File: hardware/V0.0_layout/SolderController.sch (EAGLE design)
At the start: 41 parts, among them IC3 TC10553.3V, J1 12V input, Q1 16MHz, SW1 ENCODER_SW1-PEC12, U1 ATMEGA328P-AU(R), U3 78M05

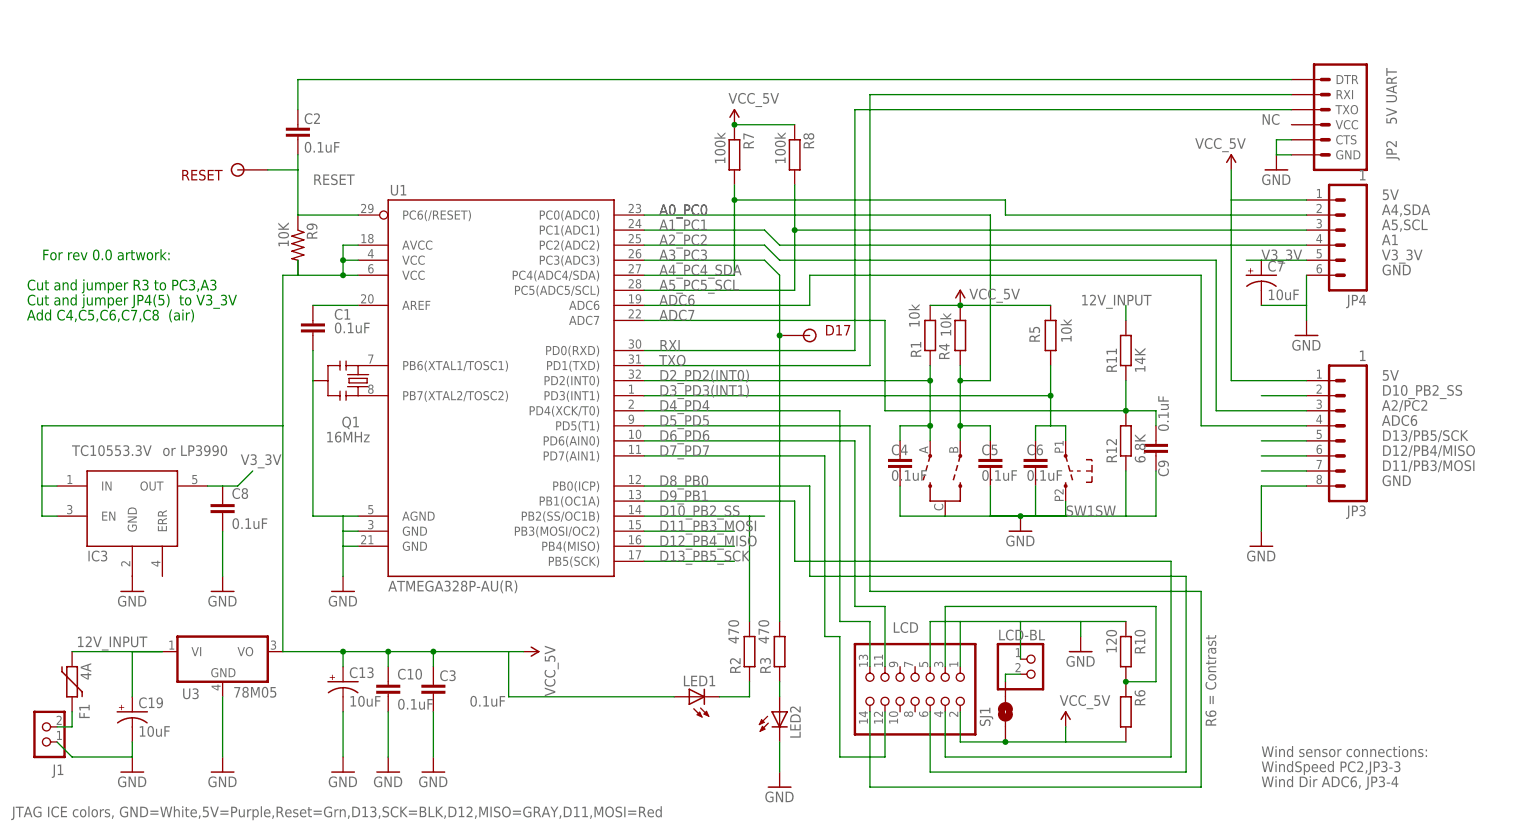
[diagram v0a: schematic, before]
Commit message: added 12_adc_daughter/LTC2495_16x_pga_adc.pdf removed eagle.epf files and added gitignore file
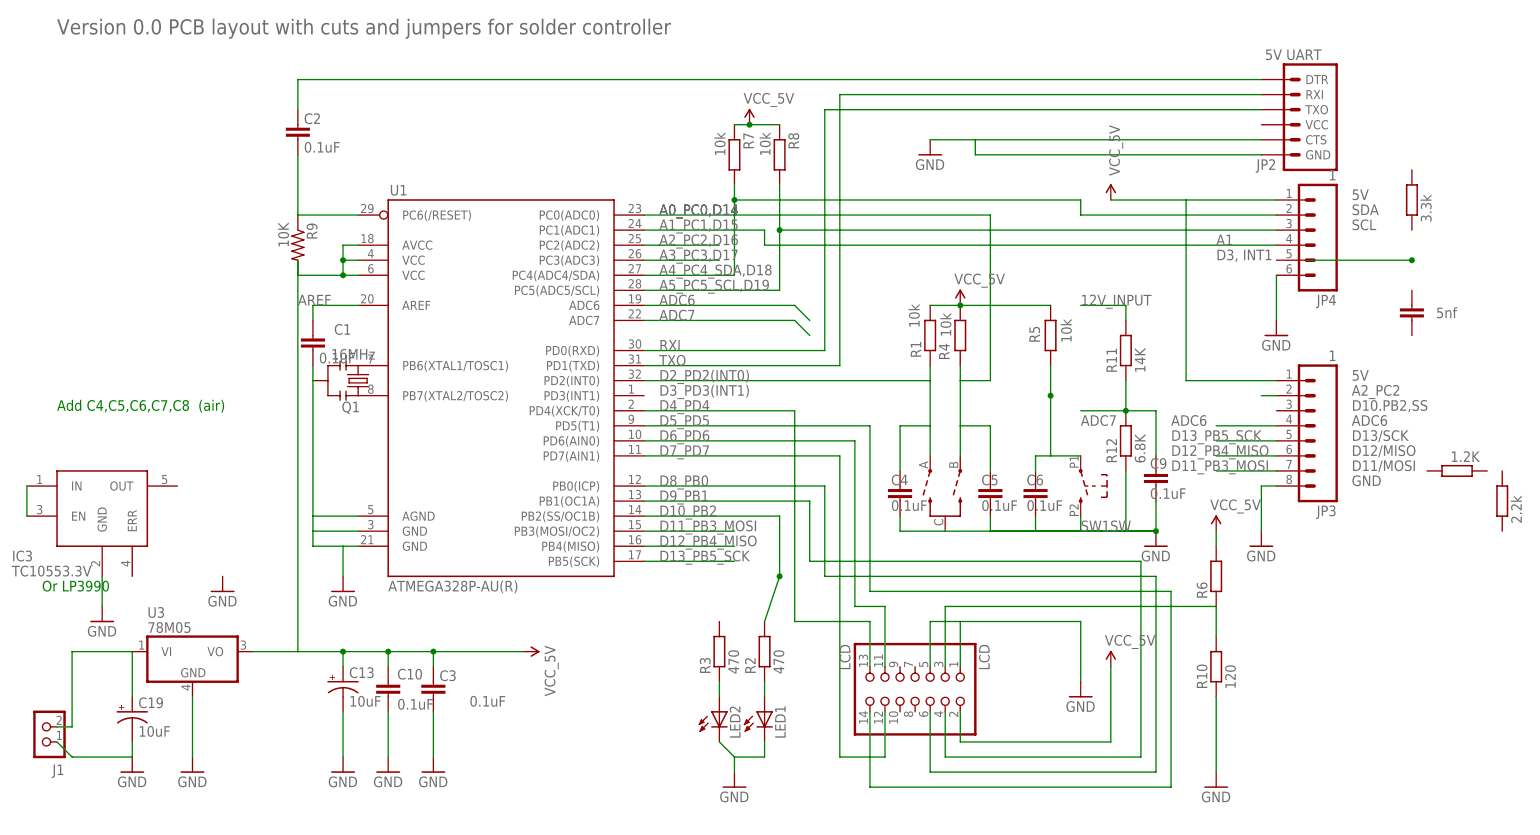
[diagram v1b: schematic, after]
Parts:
- removed C8: 0.1uF, SparkFun:CAP0805
- removed D17: D17-A3-PC3, 1AA_Stofer:SOLDER_POINTA
- removed F1: 4A, dp_devices:FUSE_PTC-0805
- removed LCD-BL: (no value), 1AA_Stofer:PINHD-1X2
- removed RESET: SOLDER_POINTA, 1AA_Stofer:SOLDER_POINTA
- removed SJ1: BACKLIGHT, SparkFun-Passives:SOLDERJUMPERNO
- added R13: 1.2K, dp_devices:RESISTOR-0603
- added R14: 2.2k, dp_devices:RESISTOR-0603
- added R15: 3.3k, dp_devices:RESISTOR-0603
- C7: value 10uF -> 5nf; device SparkFun:CAP_POL1206 -> SparkFun:CAP0805
- R7, R8: value 100k -> 10k
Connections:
- net A0_PC0 renamed A0_PC0,D14
- net A1_PC1 renamed A1_PC1,D15
- net A4_PC4_SDA renamed A4_PC4_SDA,D18
- net A5_PC5_SCL renamed A5_PC5_SCL,D19
- removed net A3_PC3: D17.P$1, R3.2, U1.PC3(ADC3)
- removed net D10_PB2_SS: JP3.2, R2.2, U1.PB2(SS/OC1B)
- removed net N$11: F1.1, J1.2
- removed net V3_3V: C7.+, C8.1, IC3.OUT, JP4.5
- new net A2_PC2,D16: U1.PC2(ADC2)
- new net A3_PC3,D17: U1.PC3(ADC3)
- new net D10_PB2: R2.2, U1.PB2(SS/OC1B)
- net 12V_INPUT: now also J1.2; no longer F1.2
- net 5V: no longer IC3.EN, IC3.IN, LED1.A, SJ1.1
- net A2_PC2: now also JP3.2; no longer JP3.3, U1.PC2(ADC2)
- net D3_PD3(INT1): no longer U1.PD3(INT1)
- net GND: now also LED1.C; no longer C7.-, C8.2, LCD-BL.1
- net N$12: now also IC3.EN, IC3.IN; no longer LED1.C, R2.1
- net N$13: now also LED1.A, R2.1; no longer LCD-BL.2, SJ1.2
- net RESET: no longer RESET.P$1
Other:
- note added: "+"
- note added: "AC_CTRL: See ReflowHaeterTriac.sch"
- note added: "AC_Control Zero X-ing"
- note added: "AC_Control_GND"
- note added: "AC_Control_Triac"
- note added: "Cut trace"
- note added: "D10.PB2,SS"
- note added: "D11/MOSI"
- note added: "D12/MISO"
- note added: "D13/SCK"
- note added: "D3, INT1"
- note added: "High wire"
- note added: "KMR-1.8 SPI orAdafruit"
- note added: "LCD : 1.8 SPI TFT 128x160"
- note added: "LCD led: Some boards need an external 92ohm resistor from 5V"
- note added: "LCD+5V"
- note added: "LCD_GND"
- note added: "Or LP3990"
- note added: "PIN_BEEPER"
- note added: "PIN_LCD_CS"
- note added: "PIN_LCD_D/C, A0"
- note added: "PIN_LCD_RST"
- note added: "PIN_LCD_SCK"
- note added: "PIN_LCD_SDA"
- note added: "PIN_TC_CS"
- note added: "PIN_TC_DO"
- note added: "PIN_TC_SCK"
- note added: "R6 could be used for that if R10 is removed"
- note added: "SCL"
- note added: "SDA"
- note added: "TC_+5V"
- note added: "TC_GND"
- note added: "TC_adapter : MAX_6675"
- note added: "Version 0.0 PCB layout with cuts and jumpers for solder controller"
- note added: "X"
- note added: "x"
- note removed: "A2/PC2"
- note removed: "A4,SDA"
- note removed: "A5,SCL"
- note removed: "Cut and jumper JP4(5) to V3_3V"
- note removed: "Cut and jumper R3 to PC3,A3"
- note removed: "D11/PB3/MOSI"
- note removed: "D12/PB4/MISO"
- note removed: "D13/PB5/SCK"
- note removed: "For rev 0.0 artwork:"
- note removed: "JTAG ICE colors, GND=White,5V=Purple,Reset=Grn,D13,SCK=BLK,D12,MISO=GRAY,D11,MOSI=Red"
- note removed: "NC"
- note removed: "R6 = Contrast"
- note removed: "Wind Dir ADC6, JP3-4"
- note removed: "Wind sensor connections:"
- note removed: "WindSpeed PC2,JP3-3"
- note removed: "or LP3990"
- moved on the sheet: C1, C4, C5, C6, C9, IC3, JP2, JP3, JP4, LED1, LED2, R10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
